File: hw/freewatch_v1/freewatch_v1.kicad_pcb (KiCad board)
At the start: 2 copper layers, 40.6 x 40.6 mm, 108 parts, among them P1 USB-MICRO-AB, P2 CONN_1, P3 CONN_2, P4 CONN_1, P5 CONN_1, P6 CONN_2, P7 CONN_6, SW1 SW_PUSH, SW2 SW_PUSH, SW3 SW_PUSH, SW4 SW_PUSH, U1 PRTR5V0U2X, U10 MAX44009, U11 LSM303C, U12 MPL3115A2, U13 ADP198, U14 LS013B7DH03, U15 EFM32GG330, U2 bq24072, U3 TPS780180300, U4 MAX17047, U5 MAX2659, U6 L70, U7 MICRO_SDCARD_SPI, U8 ADP198, U9 ADP198, X1 CRYSTAL_SMD

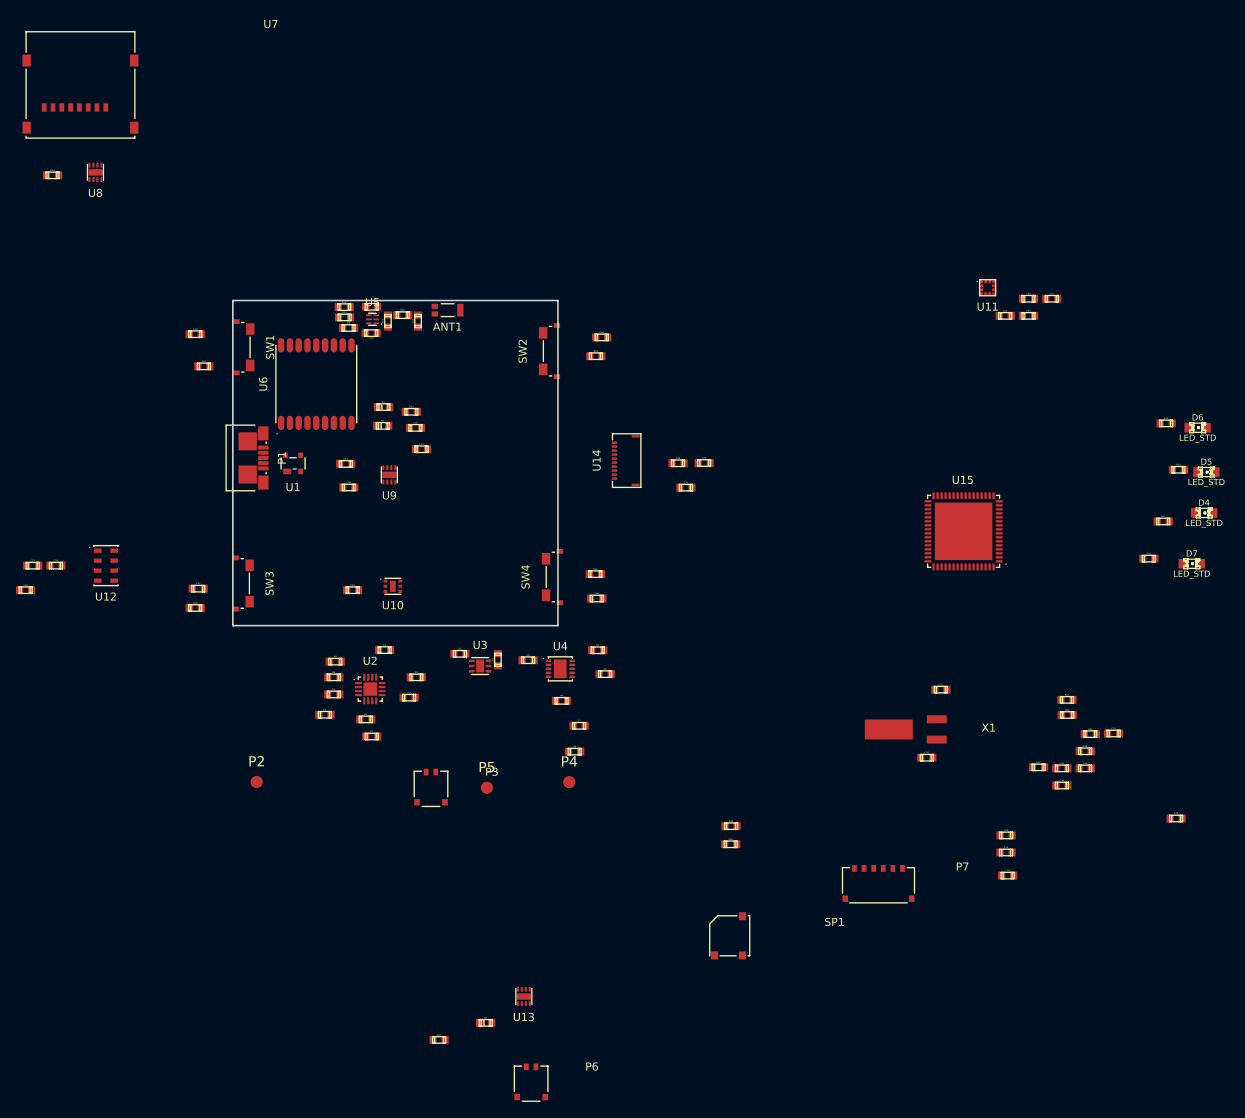
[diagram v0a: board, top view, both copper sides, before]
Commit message: hw: Continue placement, start routing, fix some bug in symbols.
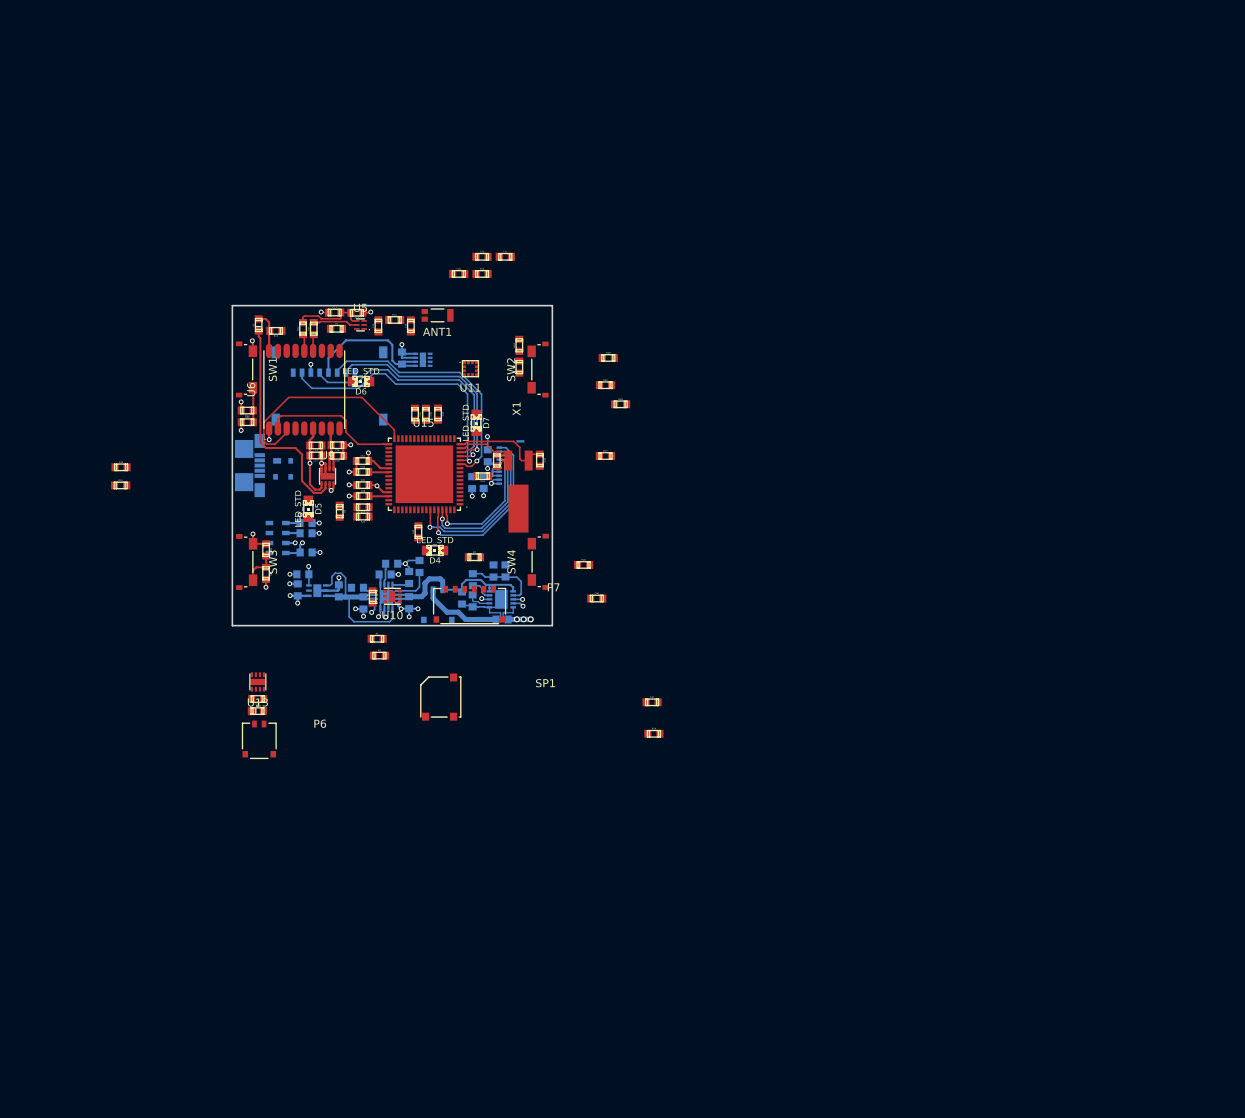
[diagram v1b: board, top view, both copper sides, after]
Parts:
- removed P2, P4, P5: CONN_1, Measurement_Points:Measurement_Point_Round-SMD-Pad_Small
- added R27: 10k, freewatch_footprints:r_0603, B.Cu at (109.7, 106.9)
- added R28: 10k, freewatch_footprints:r_0603, B.Cu at (120.4, 107.5)
- C1, C14, C2, C24, C25, C26, C28, C29, C3, C30, C4, C5, C6, C7, C8, P1, P3, R3, R4, R5, R6, R8, R9, U1, U12, U14, U2, U3, U4, U7, U8: moved to B.Cu
- moved D5 112.3 mm to (95.8, 99.7), turned to 270 degrees
- moved D6 104.7 mm to (102.4, 83.8), turned to 180 degrees
- moved C35 98.8 mm to (102.6, 96.7)
- moved C33 97.6 mm to (102.6, 95.1)
- moved D4 96.2 mm to (111.6, 104.9), turned to 180 degrees
- moved C36 94.6 mm to (102.6, 98.1)
- moved C34 94.2 mm to (102.6, 93.7)
- moved C38 93.7 mm to (109.1, 87.9), turned to 270 degrees
- moved C39 92.8 mm to (110.5, 87.9), turned to 270 degrees
- moved R22 91.5 mm to (102.6, 100.7), turned to 180 degrees
- moved R21 91.2 mm to (102.6, 99.5), turned to 180 degrees
- moved D7 91.2 mm to (116.8, 89.0), turned to 270 degrees
- moved R16 88.5 mm to (72.3, 96.8)
- moved R15 88.5 mm to (72.4, 94.5)
- moved C40 88.4 mm to (112.0, 87.9), turned to 270 degrees
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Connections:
- C42 pad 1: Net-(C42-Pad1) -> VCC
- C5 pad 2: Net-(C5-Pad2) -> GND
- C6 pad 2: Net-(C5-Pad2) -> Net-(C6-Pad2)
- C7 pad 2: Net-(C5-Pad2) -> Net-(C6-Pad2)
- C8 pad 2: Net-(C5-Pad2) -> Net-(C6-Pad2)
- P3 pad 2: Net-(C5-Pad2) -> Net-(C6-Pad2)
- R9 pad 1: Net-(C5-Pad2) -> Net-(C6-Pad2)
- U15 pad 23: Net-(C42-Pad1) -> VCC
- U15 pad 26: Net-(C42-Pad1) -> VCC
- U15 pad 27: Net-(C42-Pad1) -> VCC
- U15 pad 55: Net-(C42-Pad1) -> VCC
- U15 pad 8: Net-(C42-Pad1) -> VCC
- U2 pad 17: (no net) -> GND
- U3 pad 7: (no net) -> GND
- U4 pad 11: Net-(C5-Pad2) -> Net-(C6-Pad2)
- U4 pad 6: Net-(C5-Pad2) -> Net-(C6-Pad2)
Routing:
- net GND: track 0.00 -> 67.7 mm, vias 0 -> 35
- net SD_MISO: track 0.00 -> 33.5 mm, vias 0 -> 1
- net SD_MOSI: track 0.00 -> 31.6 mm, vias 0 -> 1
- net SD_CLK: track 0.00 -> 31.4 mm, vias 0 -> 1
- net SD_CS_N: track 0.00 -> 27.7 mm, vias 0 -> 1
- net Net-(D1-Pad2): track 0.00 -> 27.6 mm
- net GPS_RXD: track 0.00 -> 26.8 mm
- net VCC: track 0.00 -> 26.7 mm, vias 0 -> 9
- net Net-(C2-Pad1): track 0.00 -> 25.4 mm
- net /MCU_DISPLAY/LCD_CLK: track 0.00 -> 22.3 mm, vias 0 -> 1
- net +BATT: track 0.00 -> 21.8 mm
- net /MCU_DISPLAY/LCD_DI: track 0.00 -> 21.5 mm, vias 0 -> 1
- net Net-(C6-Pad2): track 0.00 -> 19.4 mm
- net /MCU_DISPLAY/LCD_CS: track 0.00 -> 18.4 mm, vias 0 -> 1
- net Net-(C14-Pad1): track 0.00 -> 18.0 mm
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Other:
- board size 40.6 x 40.6 mm -> 40 x 40 mm
- copper layers 2 -> 4
- net class class3 added: clearance 0.254, trace_width 0.254, via_dia 1.0668, via_drill 0.6604
- net class class4 added: clearance 0.2032, trace_width 0.2032, via_dia 0.762, via_drill 0.4572
- net class class5 added: clearance 0.1778, trace_width 0.1778, via_dia 0.762, via_drill 0.4572
- net class class6 added: clearance 0.1524, trace_width 0.1524, via_dia 0.6096, via_drill 0.3556
- rule pad_to_mask_clearance: 0 -> 0.1
- rule trace_min: 0.254 -> 0.1524
- rule via_min_drill: 0.508 -> 0.3556
- rule via_min_size: 0.889 -> 0.6096

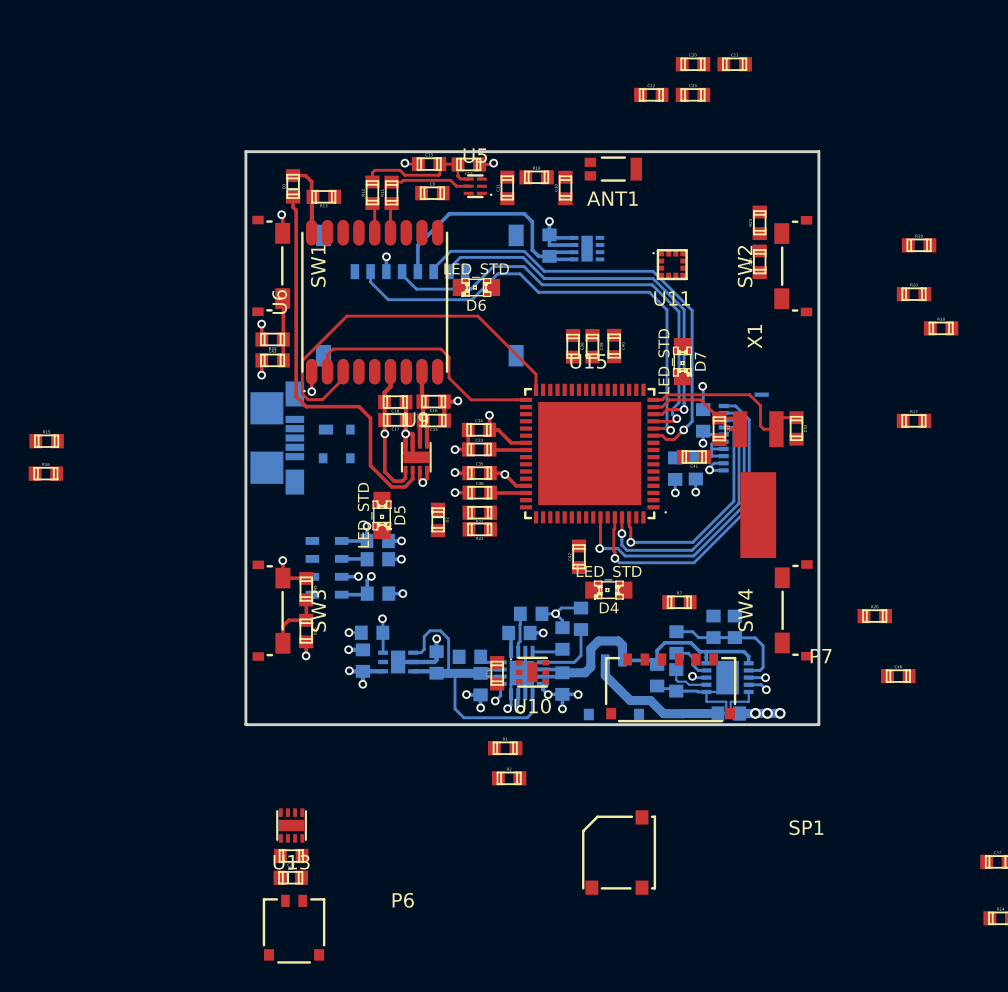
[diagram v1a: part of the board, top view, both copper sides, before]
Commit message: hw: Continue placement and routing (might change pressure sensor and LDO).
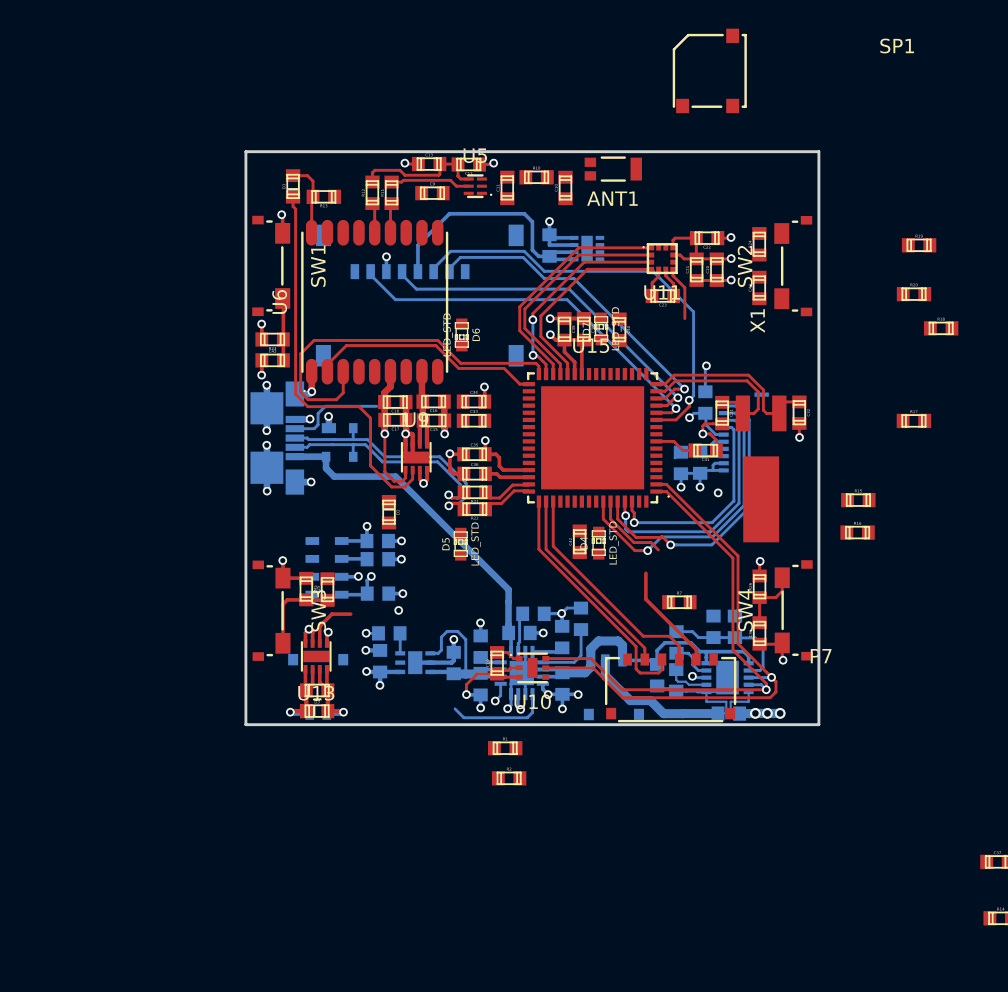
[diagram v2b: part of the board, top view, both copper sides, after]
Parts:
- D4, D5, D6, D7: footprint LEDs:LED-0805 -> LEDs:LED-0603
- P6: moved to B.Cu
- moved R15 56.8 mm to (129.1, 98.6)
- moved R16 56.8 mm to (129.0, 100.9)
- moved SP1 54.9 mm to (118.7, 68.7)
- moved C21 14.6 mm to (117.8, 82.5), turned to 90 degrees
- moved C20 14.4 mm to (119.2, 82.5), turned to 90 degrees
- moved C23 14.2 mm to (115.4, 84.4), turned to 180 degrees
- moved P6 13.2 mm to (91.3, 113.5)
- moved U13 11.9 mm to (91.2, 109.5)
- moved D3 11.8 mm to (91.3, 113.4)
- moved C27 11.7 mm to (91.3, 111.9)
- moved C22 10.7 mm to (118.5, 80.3), turned to 180 degrees
- moved C46 10.1 mm to (122.2, 107.9), turned to 90 degrees
- moved R26 8.30 mm to (122.2, 104.7), turned to 90 degrees
- moved D7 6.12 mm to (111.1, 86.7), turned to 90 degrees
- moved D5 5.85 mm to (101.3, 101.7), turned to 90 degrees
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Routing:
- net GND: track 67.7 -> 112.1 mm, vias 35 -> 47
- net SCL: track 1.18 -> 37.1 mm
- net SDA: track 1.38 -> 35.1 mm
- net +5V: track 4.25 -> 28.5 mm
- net VCC: track 26.7 -> 49.7 mm, vias 9 -> 13
- net USB_DP: track 0.00 -> 17.8 mm, vias 0 -> 1
- net /MCU_DISPLAY/SWCLK: track 0.00 -> 17.2 mm
- net USB_DM: track 0.00 -> 17.1 mm, vias 0 -> 1
- net AC_CLK: track 0.00 -> 16.6 mm
- net AC_CS_XL: track 0.00 -> 16.0 mm
- net /MCU_DISPLAY/SWDO: track 0.00 -> 15.7 mm
- net AC_CS_MAG: track 0.00 -> 14.5 mm, vias 0 -> 2
- net AC_SDIO: track 0.00 -> 13.9 mm
- net /MCU_DISPLAY/SWDIO: track 0.00 -> 13.9 mm
- net /MCU_DISPLAY/MCU_RST_N: track 0.00 -> 7.48 mm
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
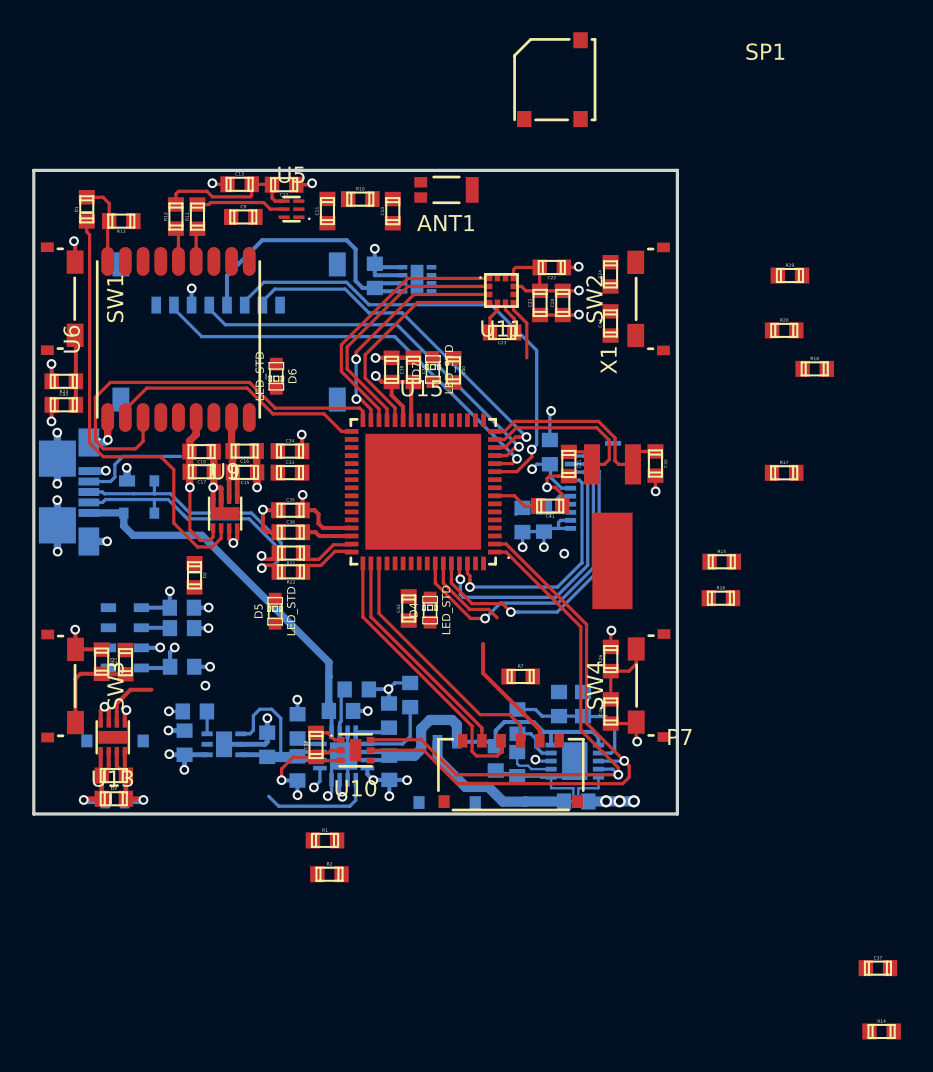
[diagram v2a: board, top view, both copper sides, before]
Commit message: hw: Change pressure sensor for MS5806-02BA, swap pins on MCU, continue routing.
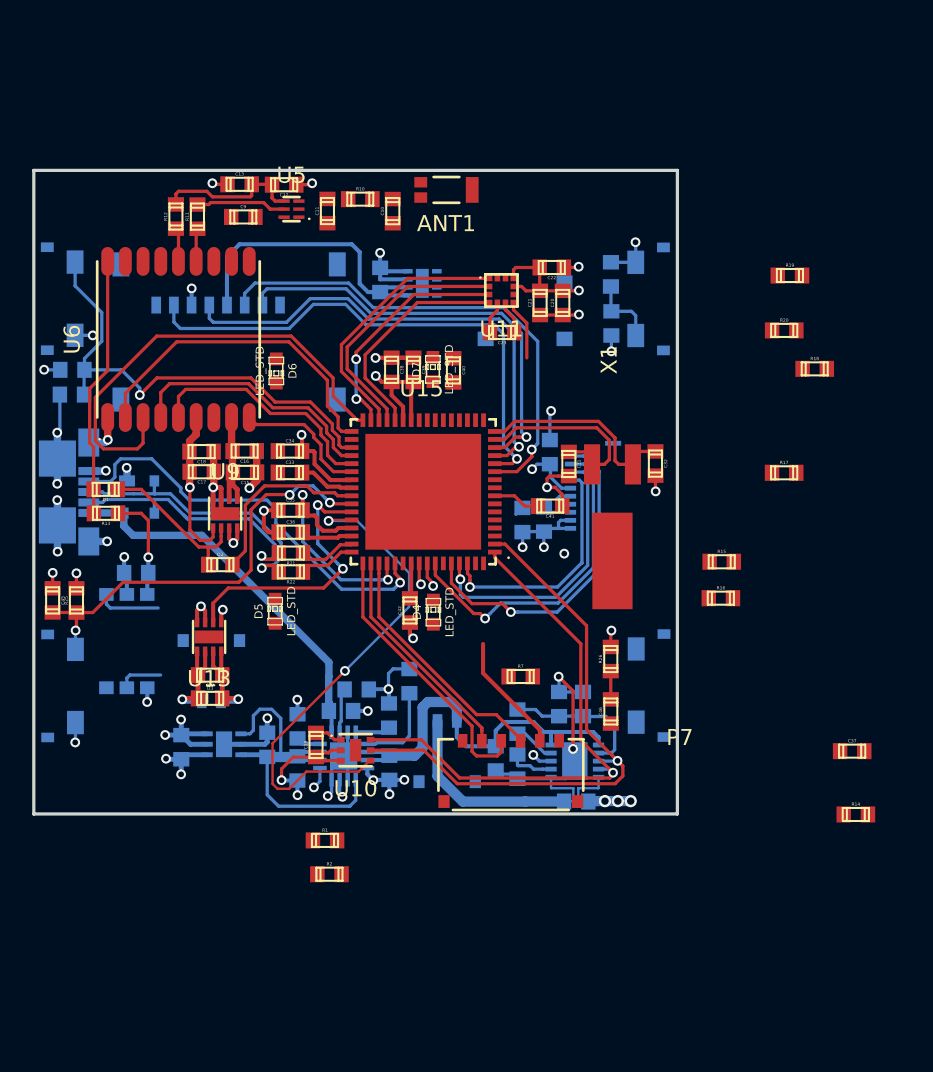
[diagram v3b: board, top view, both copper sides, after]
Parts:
- removed C24: 10uF, Capacitors_SMD:c_0603
- removed C26: 100nF, Capacitors_SMD:c_0603
- removed R3: 100k, freewatch_footprints:r_0603
- C4: value 1uF -> 4.7uF
- C43, C44, R23, R24, SP1, SW1, SW2, SW3, SW4: moved to B.Cu
- U12: value MPL3115A2 -> MS5806-02BA; footprint freewatch_footprints:LGA8 -> freewatch_footprints:MS5806-02BA
- moved R13 18.2 mm to (90.8, 95.6)
- moved D1 17.4 mm to (90.8, 94.1), turned to 180 degrees
- moved SP1 14.6 mm to (116.8, 83.2), turned to 270 degrees
- moved C37 13.6 mm to (137.2, 110.4)
- moved R14 13.6 mm to (137.4, 114.3)
- moved D3 8.65 mm to (97.3, 107.1)
- moved C27 8.65 mm to (97.3, 105.7)
- moved P6 8.65 mm to (97.3, 107.3)
- moved U13 8.65 mm to (97.2, 103.3)
- moved C25 6.49 mm to (92.7, 99.3), turned to 0 degrees
- moved R25 4.90 mm to (89.0, 101.0)
- moved C45 4.88 mm to (87.5, 101.0)
- moved R24 3.05 mm to (122.2, 83.8), turned to 270 degrees
- moved C44 3.05 mm to (122.2, 80.8), turned to 270 degrees
- moved D2 1.73 mm to (97.9, 98.8), turned to 0 degrees
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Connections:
- U12 pad 1: VCC -> SDA
- U12 pad 2: Net-(C26-Pad1) -> GND
- U12 pad 3: GND -> VCC
- U12 pad 4: VCC -> GND
- U12 pad 5: PS_INT2 -> SCL
- U12 pad 6: PS_INT1 -> Net-(U12-Pad6)
- U15 pad 10: SD_EN -> /MCU_DISPLAY/LCD_EN
- U15 pad 17: PS_INT1 -> /MCU_DISPLAY/SW_TR
- U15 pad 18: PS_INT2 -> /MCU_DISPLAY/BUZ
- U15 pad 19: V_SET -> AC_INT_XL
- U15 pad 21: BC_PGOOD_N -> AC_DRDY_MAG
- U15 pad 22: BC_CHG_N -> AC_INT_MAG
- U15 pad 24: FG_ALRT_N -> Net-(U15-Pad24)
- U15 pad 3: GPS_PPS -> FG_ALRT_N
- U15 pad 34: AC_INT_XL -> SD_EN
- U15 pad 35: AC_INT_MAG -> /MCU_DISPLAY/SW_TL
- U15 pad 36: AC_DRDY_MAG -> GPS_PPS
- U15 pad 37: Net-(U15-Pad37) -> GPS_STDBY
- U15 pad 38: /MCU_DISPLAY/SW_TL -> GPS_RST
- U15 pad 4: GPS_STDBY -> /MCU_DISPLAY/SW_BR
- U15 pad 41: /MCU_DISPLAY/BUZ -> GPS_EN
- U15 pad 42: /MCU_DISPLAY/SW_TR -> /MCU_DISPLAY/SW_BL
- U15 pad 43: /MCU_DISPLAY/SW_BL -> VM_EN
- U15 pad 44: /MCU_DISPLAY/SW_BR -> LS_INT_N
- U15 pad 5: GPS_RST -> Net-(U15-Pad5)
- U15 pad 56: VM_EN -> BC_CHG_N
- U15 pad 57: /MCU_DISPLAY/LCD_VCC -> BC_PGOOD_N
- U15 pad 59: /MCU_DISPLAY/LCD_EN -> Net-(U15-Pad59)
- U15 pad 6: GPS_EN -> Net-(U15-Pad6)
- U15 pad 7: LS_INT_N -> Net-(U15-Pad7)
- U15 pad 9: Net-(U15-Pad9) -> /MCU_DISPLAY/LCD_VCC
- U3 pad 2: Net-(U3-Pad2) -> GND
- U3 pad 3: V_SET -> GND
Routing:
- net LS_INT_N: track 0.00 -> 31.4 mm, vias 0 -> 2
- net /MCU_DISPLAY/SW_TL: track 4.34 -> 29.6 mm, vias 0 -> 1
- net /MCU_DISPLAY/SW_BL: track 5.97 -> 26.8 mm, vias 0 -> 3
- net USB_ID: track 6.82 -> 25.9 mm, vias 0 -> 1
- net Net-(D1-Pad2): track 27.5 -> 10.0 mm
- net GPS_PPS: track 0.00 -> 16.0 mm
- net GPS_STDBY: track 0.00 -> 14.9 mm
- net VM_EN: track 3.71 -> 17.0 mm, vias 0 -> 2
- net GPS_EN: track 0.00 -> 11.4 mm
- net Net-(D1-Pad1): track 5.19 -> 16.2 mm
- net +5V: track 28.5 -> 38.8 mm, vias 1 -> 2
- net Net-(C6-Pad2): track 19.4 -> 29.6 mm, vias 0 -> 2
- net VCC: track 49.7 -> 59.1 mm, vias 13 -> 14
- net GPS_RST: track 0.00 -> 8.40 mm
- net SD_MISO: track 26.9 -> 32.7 mm
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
